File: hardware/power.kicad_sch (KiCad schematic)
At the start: 96 parts, among them J3 Vcore_sel, U1 TLV62569DBV, U2 TLV62569DBV, U3 MPM3833CGRH-Z, U4 GateMate-CCGM1A1, U5 TLV62569DBV, U6 TLV62569DBV

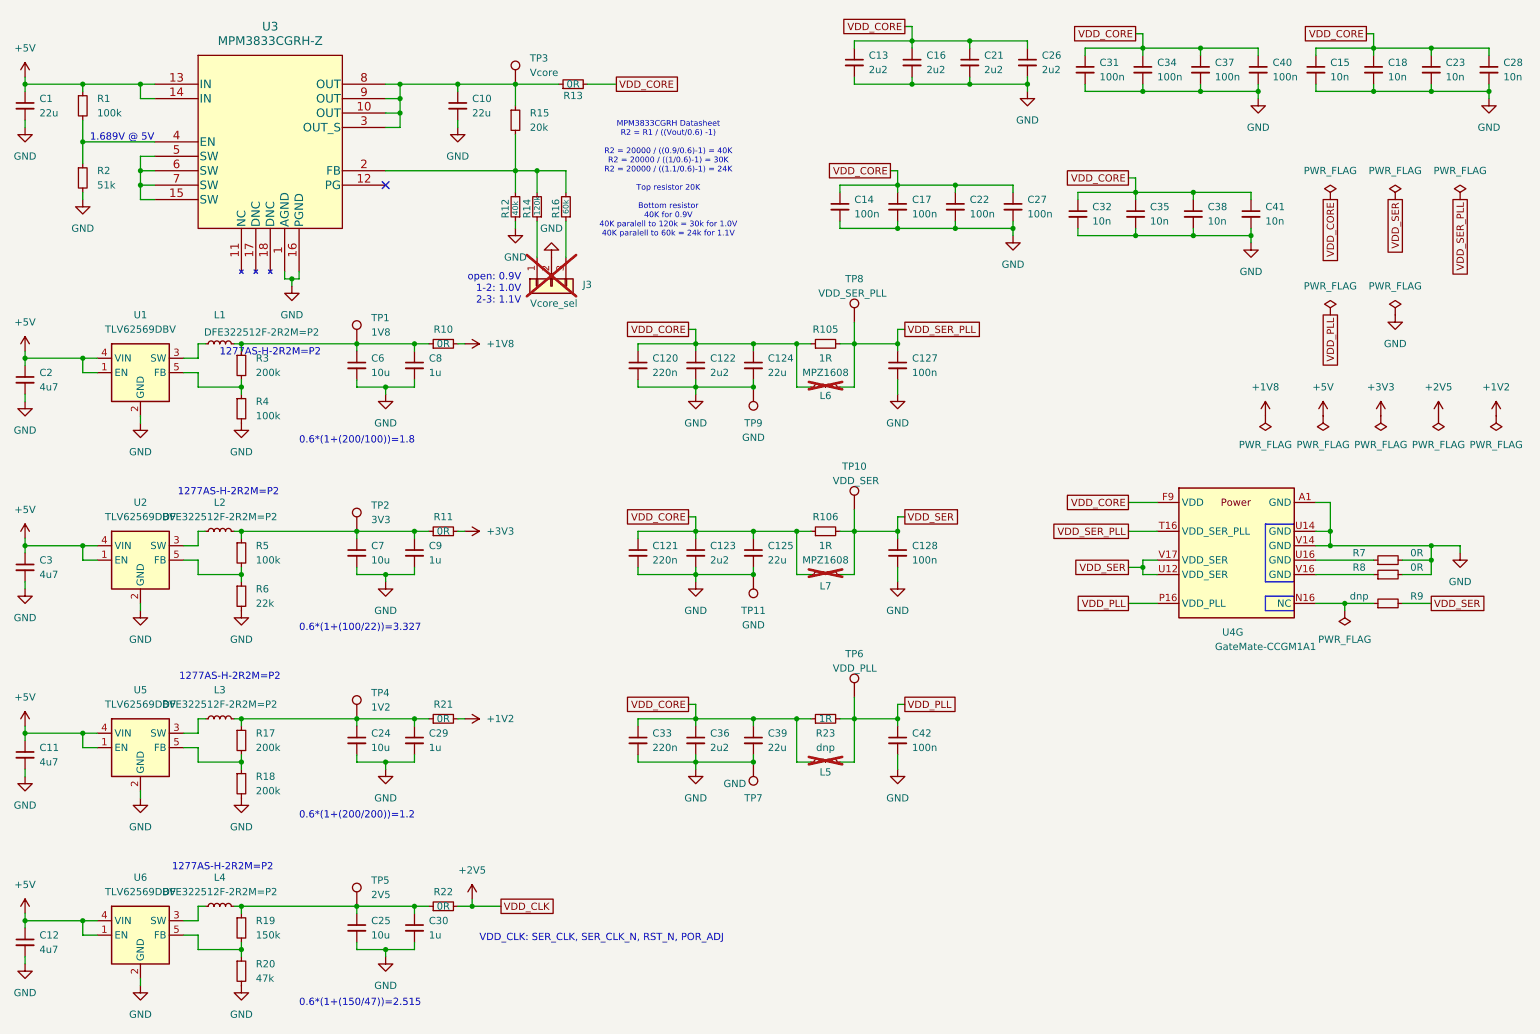
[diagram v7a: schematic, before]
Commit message: Moving VDD_CLK to 1V8, removing 2V5
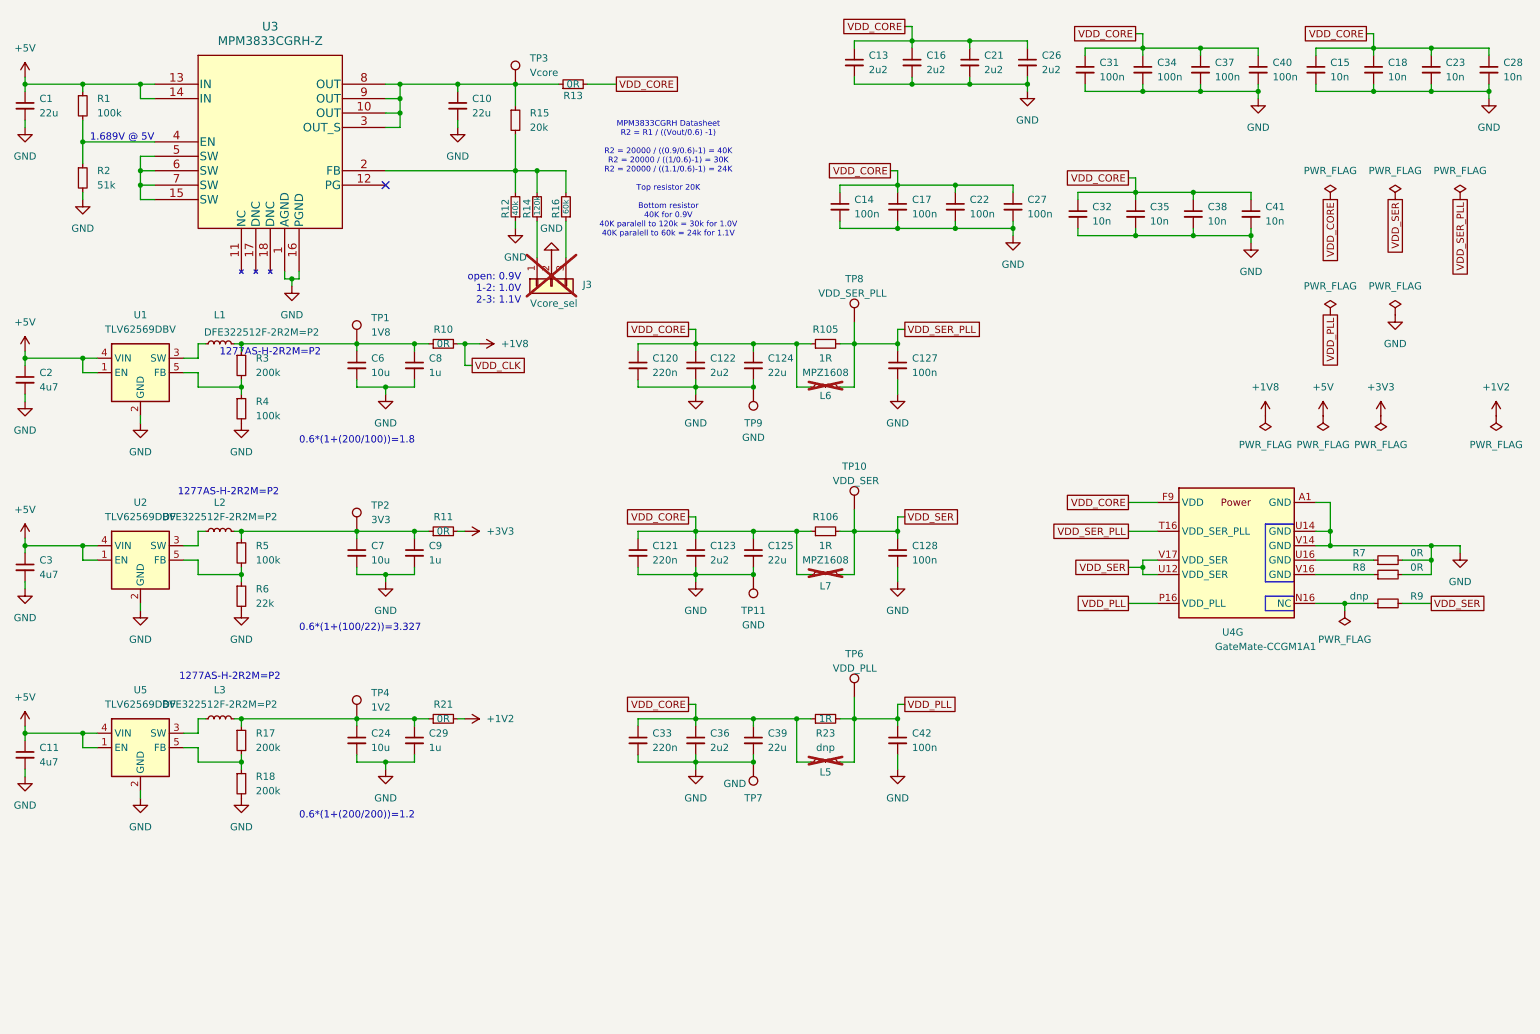
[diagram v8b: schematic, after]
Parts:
- removed C12: 4u7, Capacitor_SMD:C_0402_1005Metric, symbol Device:C_Small
- removed C25: 10u, Capacitor_SMD:C_0402_1005Metric, symbol Device:C_Small
- removed C30: 1u, Capacitor_SMD:C_0402_1005Metric, symbol Device:C_Small
- removed L4: DFE322512F-2R2M=P2, Inductor_SMD:L_1008_2520Metric, symbol Device:L_Small
- removed R19: 150k, Resistor_SMD:R_0402_1005Metric, symbol Device:R_Small
- removed R20: 47k, Resistor_SMD:R_0402_1005Metric, symbol Device:R_Small
- removed R22: 0R, Resistor_SMD:R_0603_1608Metric, symbol Device:R_Small
- removed TP5: 2V5, TestPoint:TestPoint_Pad_D1.0mm, symbol Connector:TestPoint
- removed U6: TLV62569DBV, Package_TO_SOT_SMD:SOT-23-5, symbol Regulator_Switching:TLV62569DBV
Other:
- note removed: "0.6*(1+(150/47))=2.515"
- note removed: "VDD_CLK: SER_CLK, SER_CLK_N, RST_N, POR_ADJ"
